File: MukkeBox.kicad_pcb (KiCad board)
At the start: 2 copper layers, 160 x 100 mm, 311 parts, among them J1 TB001-500-06BE CUI_Devices, J101 Conn_02x20_Odd_Even, J103 Conn_02x05_Odd_Even, J104 Conn_02x01, J301 Conn_02x04_Odd_Even, J302 Conn_02x04_Odd_Even, J303 TB001-500-06BE CUI_Devices, J601 Conn_01x03_Female, J602 Conn_02x01, J603 Conn_02x06_Odd_Even, J604 Conn_02x01, J605 Conn_02x01, Q1 2N7002, Q201 VS6412AE, Q301 2N7002, Q302 HSBB3103, Q303 2N7002, Q304 HSBB3103, Q305 VS6412AE, Q306 2N7002, Q307 BSS84, Q308 2N7002, Q309 VS6412AE, Q310 HSBB3103, Q311 HSBB3103, Q501 2N7002, U1 TPA3116D2, U102 STM32F030C6Tx_MukkeBox, U103 MCP9700, U2 TPA3116D2, U203 TPS40210, U301 BQ24610, U502 BK8000L, U503 TDA7719, U504 AP2553AW6-7, U505 JW5026, U602 JW5026, Y101 FOXSDLF/080-20

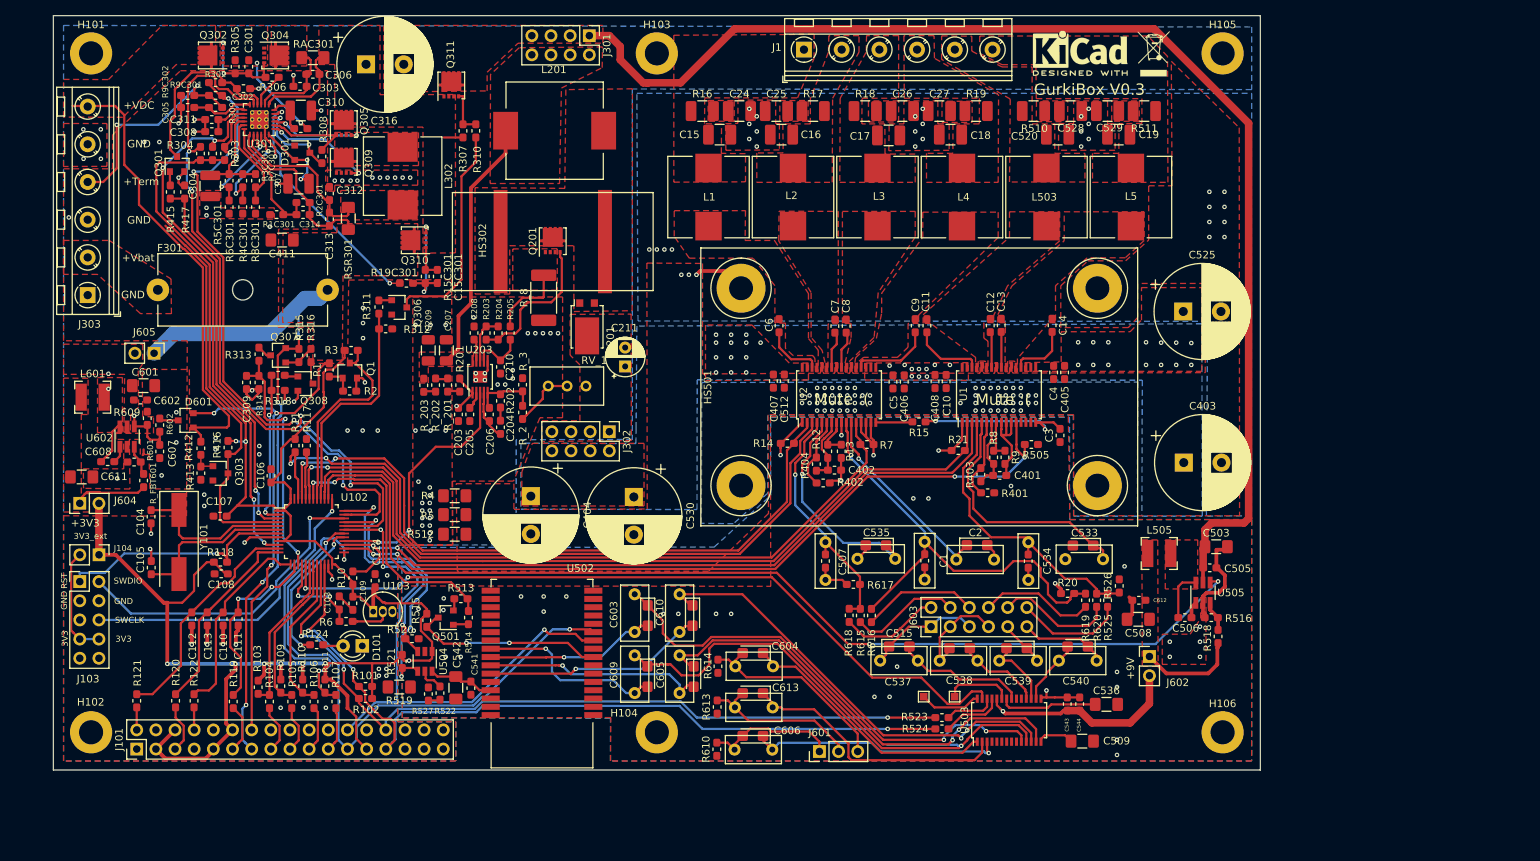
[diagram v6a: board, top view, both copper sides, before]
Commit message: I2C Dreher behoben, BOM vereinfacht, 20dB Gain an ClassD Amps
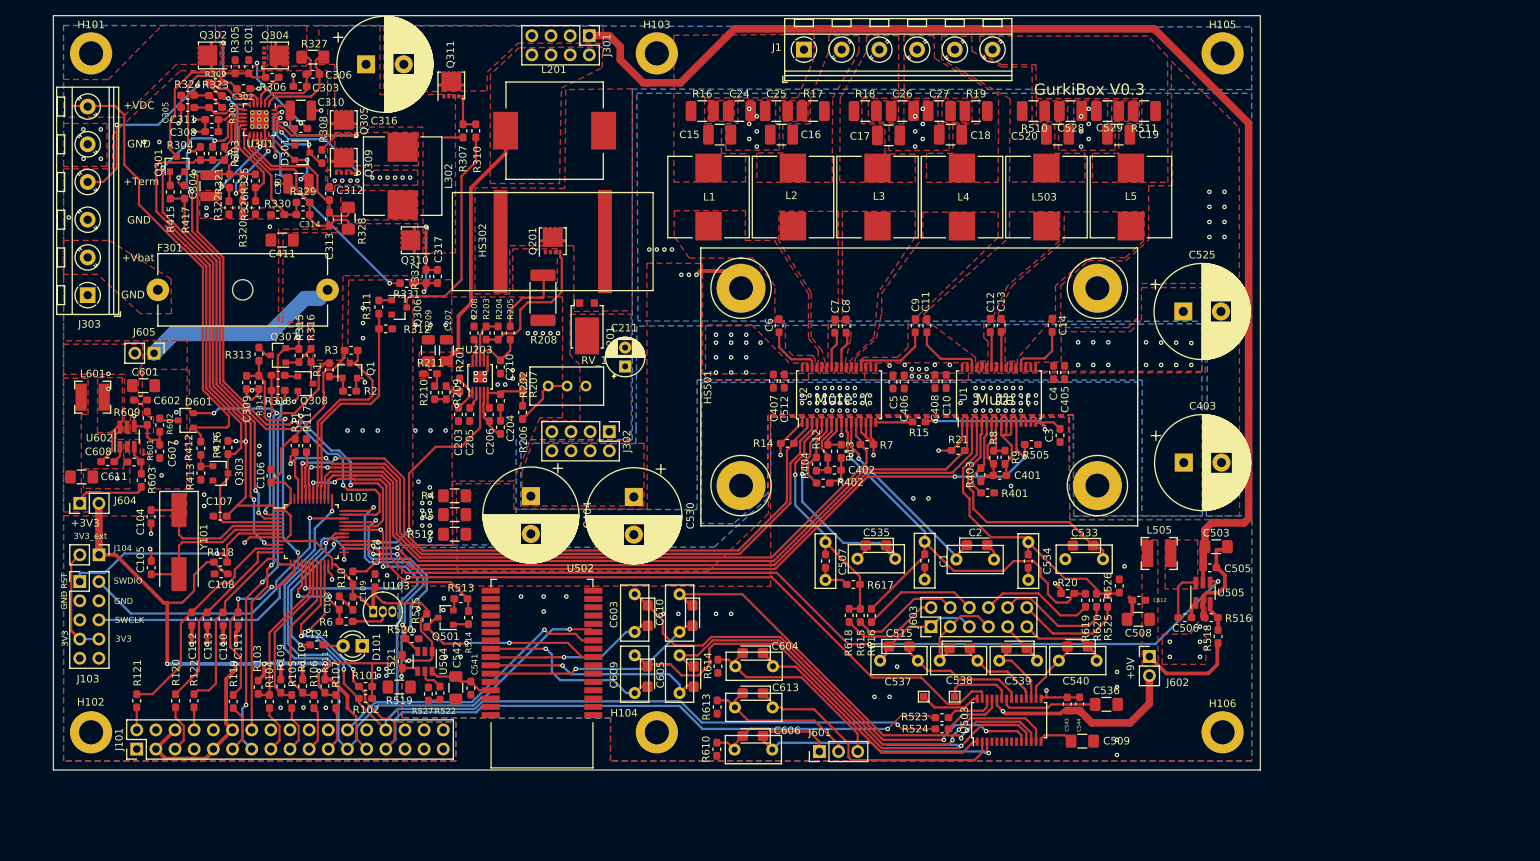
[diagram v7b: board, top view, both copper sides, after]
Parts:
- removed C15C301: 100n, Capacitor_SMD:C_0603_1608Metric_Pad1.05x0.95mm_HandSolder
- removed R15C301, R1C301, R3C301, R5C301, R7C301, R_201, R_202, R_203: 100K, Resistor_SMD:R_0603_1608Metric_Pad1.05x0.95mm_HandSolder
- removed R19C301: 1K, Resistor_SMD:R_0603_1608Metric_Pad1.05x0.95mm_HandSolder
- removed R2C301: 700K, Resistor_SMD:R_0603_1608Metric_Pad1.05x0.95mm_HandSolder
- removed R4C301: 22K, Resistor_SMD:R_0603_1608Metric_Pad1.05x0.95mm_HandSolder
- removed R6C301, R8C301, R9C301, R_FBT601: 10K, Resistor_SMD:R_0603_1608Metric_Pad1.05x0.95mm_HandSolder
- removed R9C302: 470K, Resistor_SMD:R_0603_1608Metric_Pad1.05x0.95mm_HandSolder
- removed RAC301, RSR301: 10m, Resistor_SMD:R_1206_3216Metric_Pad1.42x1.75mm_HandSolder
- removed REF**: WEEE-Logo_4.2x6mm_SilkScreen, Symbol:WEEE-Logo_4.2x6mm_SilkScreen
- removed REF**: KiCad-Logo2_5mm_SilkScreen, Symbol:KiCad-Logo2_5mm_SilkScreen
- removed R_2: 47K, Resistor_SMD:R_0603_1608Metric_Pad1.05x0.95mm_HandSolder
- removed R_3: 1K5, Resistor_SMD:R_0603_1608Metric_Pad1.05x0.95mm_HandSolder
- removed R_8: R012, Resistor_SMD:R_2512_6332Metric_Pad1.52x3.35mm_HandSolder
- added C317: 100n, Capacitor_SMD:C_0603_1608Metric_Pad1.05x0.95mm_HandSolder, F.Cu at (101.4, 66.7)
- added R206: 47K, Resistor_SMD:R_0603_1608Metric_Pad1.05x0.95mm_HandSolder, F.Cu at (112.7, 84.7)
- added R207: 1K5, Resistor_SMD:R_0603_1608Metric_Pad1.05x0.95mm_HandSolder, F.Cu at (112.7, 81.0)
- added R208: R012, Resistor_SMD:R_2512_6332Metric_Pad1.52x3.35mm_HandSolder, F.Cu at (115.4, 69.5)
- added R209: 100K, Resistor_SMD:R_0603_1608Metric_Pad1.05x0.95mm_HandSolder, F.Cu at (102.5, 82.1)
- added R210: 100K, Resistor_SMD:R_0603_1608Metric_Pad1.05x0.95mm_HandSolder, F.Cu at (101.0, 82.1)
- added R211: 100K, Resistor_SMD:R_0603_1608Metric_Pad1.05x0.95mm_HandSolder, F.Cu at (100.4, 79.6)
- added R319: 100K, Resistor_SMD:R_0603_1608Metric_Pad1.05x0.95mm_HandSolder, F.Cu at (75.6, 54.0)
- added R320: 22K, Resistor_SMD:R_0603_1608Metric_Pad1.05x0.95mm_HandSolder, F.Cu at (75.6, 57.5)
- added R321: 100K, Resistor_SMD:R_0603_1608Metric_Pad1.05x0.95mm_HandSolder, F.Cu at (73.8, 54.0)
- added R322: 10K, Resistor_SMD:R_0603_1608Metric_Pad1.05x0.95mm_HandSolder, F.Cu at (73.7, 57.5)
- added R323: 10K, Resistor_SMD:R_0603_1608Metric_Pad1.05x0.95mm_HandSolder, F.Cu at (72.0, 42.7)
- added R324: 470K, Resistor_SMD:R_0603_1608Metric_Pad1.05x0.95mm_HandSolder, F.Cu at (68.3, 42.6)
- added R325: 100K, Resistor_SMD:R_0603_1608Metric_Pad1.05x0.95mm_HandSolder, F.Cu at (77.2, 54.0)
- added R326: 10K, Resistor_SMD:R_0603_1608Metric_Pad1.05x0.95mm_HandSolder, F.Cu at (77.3, 57.5)
- added R327: 10m, Resistor_SMD:R_1206_3216Metric_Pad1.42x1.75mm_HandSolder, F.Cu at (84.9, 37.6)
- added R328: 10m, Resistor_SMD:R_1206_3216Metric_Pad1.42x1.75mm_HandSolder, F.Cu at (89.6, 58.9)
- added R329: 700K, Resistor_SMD:R_0603_1608Metric_Pad1.05x0.95mm_HandSolder, F.Cu at (83.6, 56.8)
- added R330: 100K, Resistor_SMD:R_0603_1608Metric_Pad1.05x0.95mm_HandSolder, F.Cu at (80.2, 58.5)
- added R331: 1K, Resistor_SMD:R_0603_1608Metric_Pad1.05x0.95mm_HandSolder, F.Cu at (97.3, 67.6)
- added R332: 100K, Resistor_SMD:R_0603_1608Metric_Pad1.05x0.95mm_HandSolder, F.Cu at (99.9, 66.7)
- added R603: 10K, Resistor_SMD:R_0603_1608Metric_Pad1.05x0.95mm_HandSolder, F.Cu at (62.1, 93.7)
- C207, C209: value 330n -> 220n
- C308: value 33n -> 100n
- C311: value 33n -> DNP
- C314: value 22p -> 100p
- C405, C406, C407, C408: value 1n -> 100n
- C537: value 1u -> 1000p
- C604, C606, C613: value 1u -> 1u DNP
- J601: value Conn_01x03_Female -> DNP
- R12, R613, R614: value 100K -> DNP
- R13: value 20K -> 10K
- R523, R524: value 100R -> 47R
- R525, R615, R616, R619, R620: value 1K -> 0R
- R610: value 100R -> DNP
- R618: value 1K -> OR
- R9: value 75K -> 47K
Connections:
- R523 pad 1: SCL -> SDA
- R524 pad 1: SDA -> SCL
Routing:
- net Net-(R210-Pad2): track 0.00 -> 1.75 mm
- net Net-(R_201-Pad1): track 1.60 -> 0.00 mm
- net Net-(R_202-Pad2): track 1.58 -> 0.00 mm
- net Net-(R209-Pad1): track 0.00 -> 1.52 mm
- net SDA: track 109.7 -> 110.6 mm
- net SCL: track 105.3 -> 105.9 mm
- net Net-(R201-Pad2): track 1.60 -> 2.10 mm
